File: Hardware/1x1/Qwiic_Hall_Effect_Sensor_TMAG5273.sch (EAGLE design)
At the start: 31 parts, among them J1 QWIIC_RIGHT_ANGLE, J2 QWIIC_RIGHT_ANGLE, Q1 20V/4.2A/52mΩ/1.4W, U1 TMAG5273

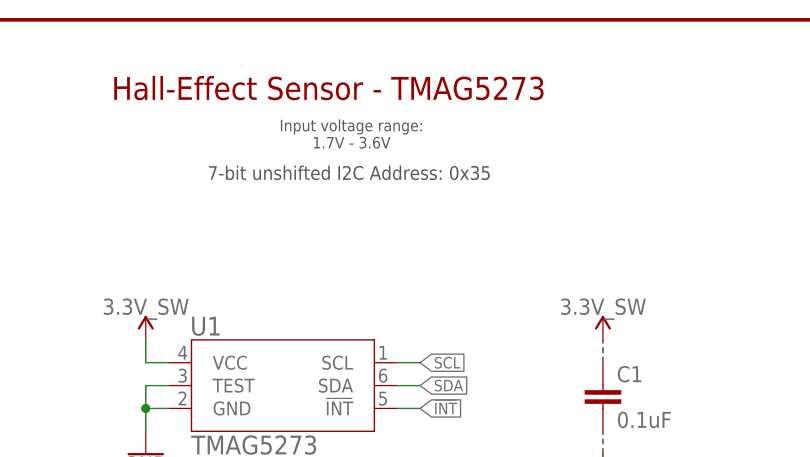
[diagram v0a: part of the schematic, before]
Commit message: Updated I2C address in schematic
Updated the I2C address to the actual address used in the library/for the devices usage
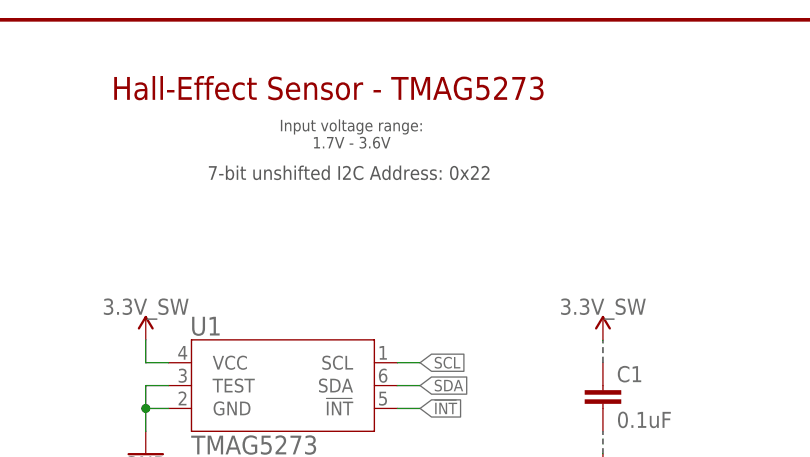
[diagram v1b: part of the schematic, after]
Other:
- note added: "7-bit unshifted I2C Address: 0x22"
- note removed: "7-bit unshifted I2C Address: 0x35"
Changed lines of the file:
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@@
 <sheet>
 <plain>
-<text x="123.698" y="167.64" size="1.524" layer="97" font="vector">7-bit unshifted I2C Address: 0x35</text>
+<text x="123.698" y="167.64" size="1.524" layer="97" font="vector">7-bit unshifted I2C Address: 0x22</text>
 <text x="137.16" y="177.8" size="2.54" layer="94" font="vector" align="center">Hall-Effect Sensor - TMAG5273</text>
 <text x="226.06" y="177.8" size="2.54" layer="94" font="vector" align="center">I²C Pullup</text>
